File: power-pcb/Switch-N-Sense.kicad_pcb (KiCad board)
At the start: 2 copper layers, 94 x 57.5 mm, 44 parts, among them P1 CONN_01X01, P2 CONN_01X01, P3 CONN_01X01, P4 CONN_01X01, P5 CONN_01X01, P6 Conn_Switch-N-Sense, Q1 CSD18540Q5B, Q2 CSD18540Q5B, Q3 CSD18540Q5B, Q4 CSD18540Q5B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

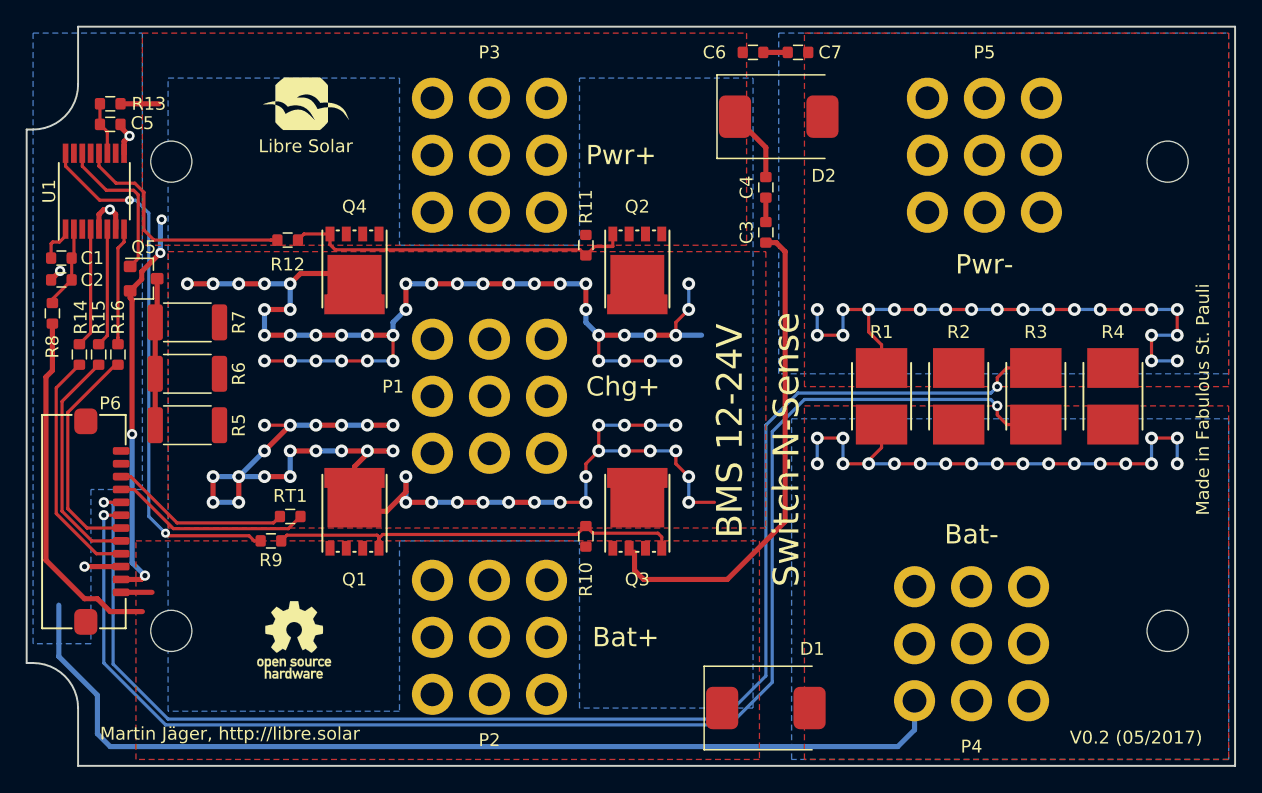
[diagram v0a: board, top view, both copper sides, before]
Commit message: Update to KiCAD 5 and minor changes in part selection
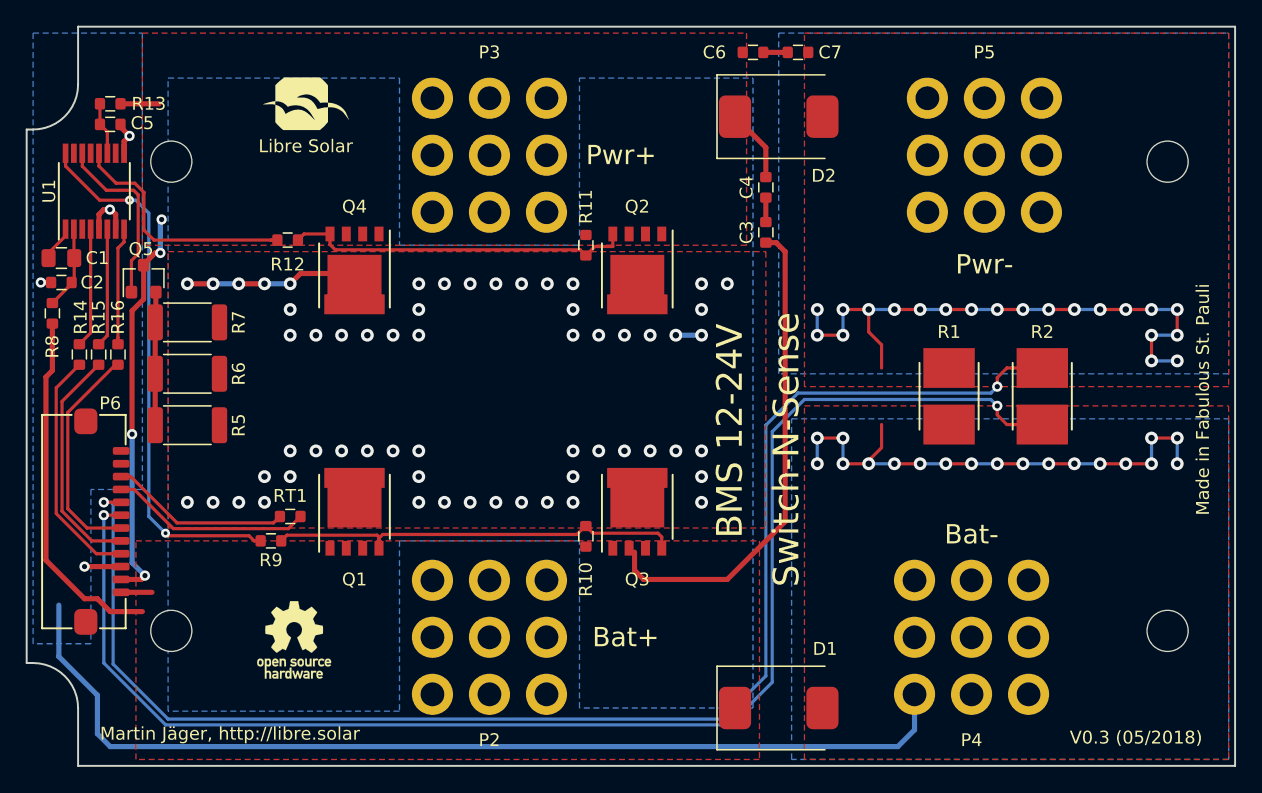
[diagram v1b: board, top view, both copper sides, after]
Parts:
- removed P1: CONN_01X01, LibreSolar:Wuerth_WP-THRBU
- removed R3, R4: 2m, LibreSolar:R_Bourns_CRE2512
- C1: footprint LibreSolar:C_0603_1608 -> LibreSolar:C_0805_2012
- D1, D2: value SMCJ36A -> SMCJ24A
- LOGO2: footprint Symbols:OSHW-Logo_5.7x6mm_SilkScreen -> Symbol:OSHW-Logo_5.7x6mm_SilkScreen
- Q1, Q2, Q3, Q4: value CSD18540Q5B -> BSC014N04LS
- Q5: value ZXMP10A13F -> ZXMP6A13F
- REF** (x4): footprint Mounting_Holes:MountingHole_3.2mm_M3 -> MountingHole:MountingHole_3.2mm_M3
- U1: footprint Housings_SSOP:TSSOP-16_4.4x5mm_Pitch0.65mm -> Package_SO:TSSOP-16_4.4x5mm_P0.65mm
- moved R2 6.50 mm to (175.5, 88.8)
- moved R1 5.25 mm to (168.2, 88.8)
- moved D1 1.00 mm to (155.0, 113.0)
- moved P4 0.50 mm to (170.0, 107.5)
- moved C2 0.20 mm to (99.2, 79.9)
- turned Q5 to 90 degrees
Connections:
- Q5 pad 2: /LOAD+ -> Net-(Q5-Pad2)
- Q5 pad 3: Net-(Q5-Pad3) -> /LOAD+
- R5 pad 1: Net-(Q5-Pad3) -> Net-(Q5-Pad2)
- R6 pad 1: Net-(Q5-Pad3) -> Net-(Q5-Pad2)
- R7 pad 1: Net-(Q5-Pad3) -> Net-(Q5-Pad2)
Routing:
- net /CHG+: track 173.6 -> 15.3 mm, vias 77 -> 59
- net Net-(Q5-Pad3): track 11.5 -> 0.00 mm
- net Net-(Q5-Pad2): track 0.00 -> 10.6 mm
- net /PCHG_G: track 12.1 -> 14.1 mm
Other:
- board text added: "V0.3 (05/2018)"
- board text removed: "Chg+"
- board text removed: "V0.2 (05/2017)"
